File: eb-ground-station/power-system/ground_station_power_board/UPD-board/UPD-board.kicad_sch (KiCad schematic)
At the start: 96 parts, among them J1 Conn_01x04, J10 PI 1827486, J2 Conn_01x03, J3 Conn_01x06, J4 Conn_01x06, J5 Conn_01x06, J6 Conn_01x06, J7 PI 1809131, J8 PI 1827923, J9 PI 1827486, Q21 SUD50P08-25L-E3, Q22 SUD50P08-25L-E3, U1 MAX7310ATE, U2 MAX7310ATE, U3 MAX7310ATE, U4 MCP9808, U5 ADS1115IDGS, U6 UA78M33, U7 U_RasPi_40pin

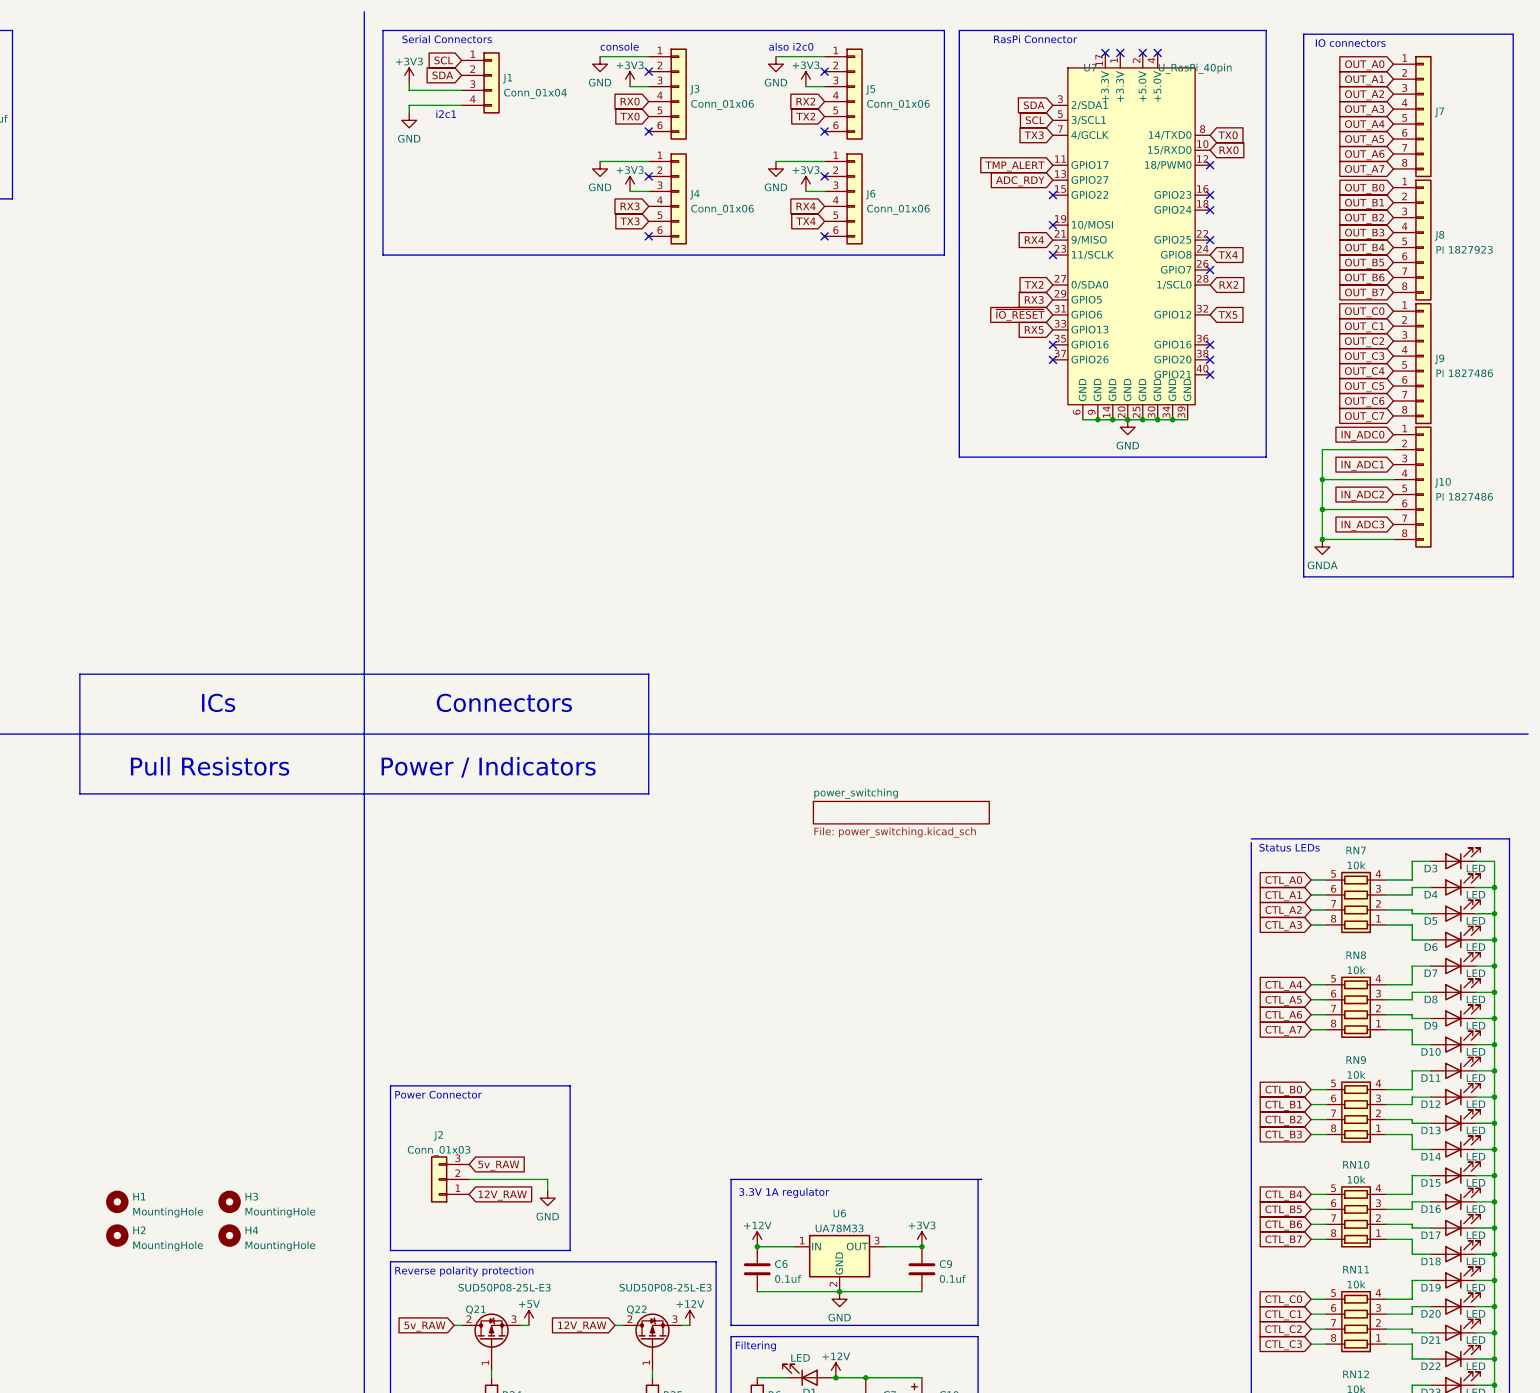
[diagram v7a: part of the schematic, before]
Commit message: Fixed some issues and added propper power input connector
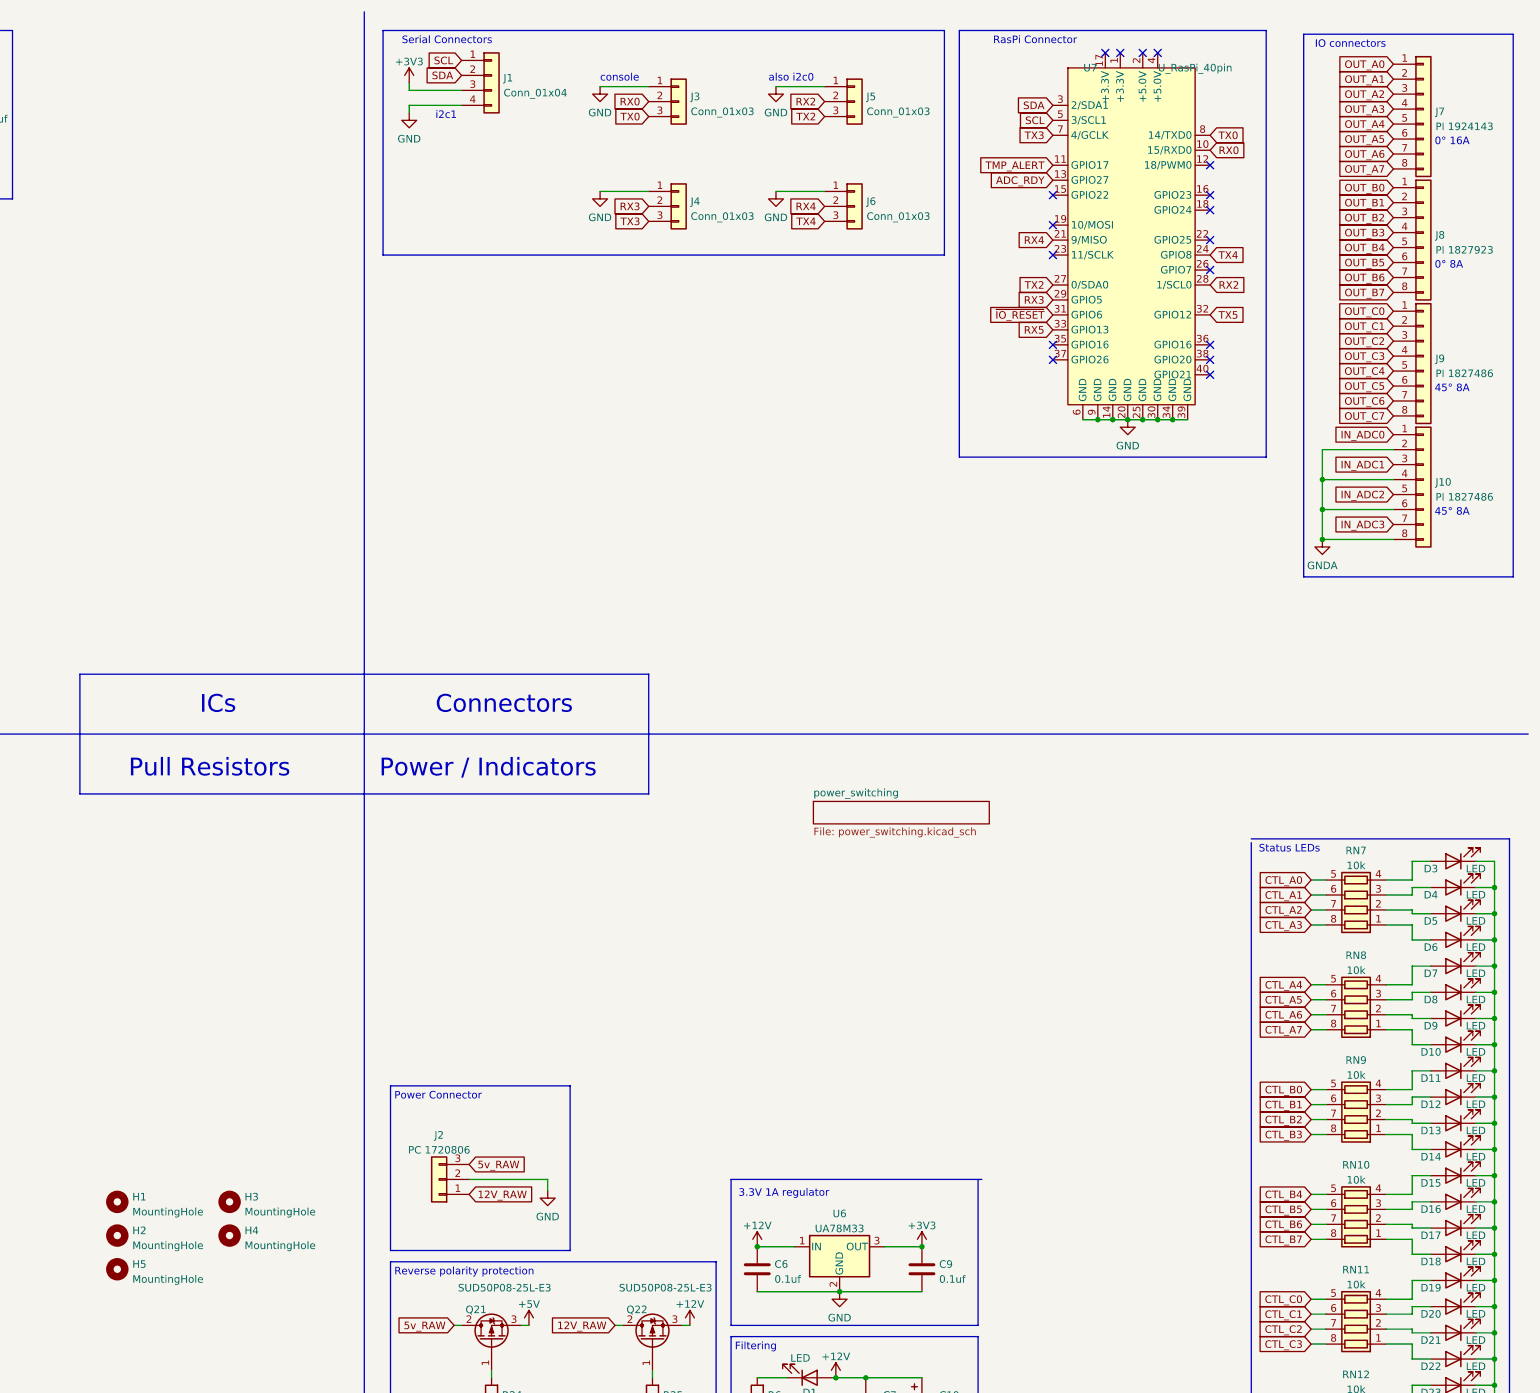
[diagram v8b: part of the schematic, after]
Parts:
- removed J3, J4, J5, J6: Conn_01x06, Connector_PinHeader_2.54mm:PinHeader_1x06_P2.54mm_Vertical, symbol Connector_Generic:Conn_01x06
- added H5: MountingHole, oresat-footprints:H-MCMASTER-94100A150, symbol Mechanical:MountingHole
- added J3, J4, J5, J6: Conn_01x03, Connector_PinHeader_2.54mm:PinHeader_1x03_P2.54mm_Vertical, symbol Connector_Generic:Conn_01x03
- J2: value Conn_01x03 -> PC 1720806; footprint Connector_Phoenix_MC_HighVoltage:PhoenixContact_MC_1,5_3-GF-5.08_1x03_P5.08mm_Horizontal_ThreadedFlange_MountHole -> oresat-footprints:PhoenixContact_GMSTBA_2,5_3-G-7,62_1x03_P7.62mm_Horizontal
- J7: value PI 1809131 -> PI 1924143
- J8: footprint Connector_Phoenix_MC:PhoenixContact_MC_1,5_8-GF-3.81_1x08_P3.81mm_Horizontal_ThreadedFlange -> oresat-footprints:PhoenixContact_MC_1,5_8-GF-3.81_1x08_P3.81mm_Horizontal_ThreadedFlange
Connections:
- net GND: now also J3.1 (Pin_1), J4.1 (Pin_1), J5.1 (Pin_1), J6.1 (Pin_1)
- net RX0: now also J3.2 (Pin_2)
- net RX2: now also J5.2 (Pin_2)
- net RX3: now also J4.2 (Pin_2)
- net RX4: now also J6.2 (Pin_2)
- net TX0: now also J3.3 (Pin_3)
- net TX2: now also J5.3 (Pin_3)
- net TX3: now also J4.3 (Pin_3)
- net TX4: now also J6.3 (Pin_3)
- no-connect marks 25 -> 17
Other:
- note added: "0° 16A"
- note added: "0° 8A"
- note added: "45° 8A"
